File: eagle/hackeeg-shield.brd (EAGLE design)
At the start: 101.6 x 53.3 mm, 144 parts, among them IC1 ADS1299IPAG, IC10 TXB0108PWR, IC11 TXB0108PWR, IC2 TPS72325DBVT, IC3 TPS73225DBVT, IC5 24AA256UID, IC6 TPS60403DBVT, IC7 OPA376DBV, IC8 OPA376DBV, IC9 TXS0102DCUR

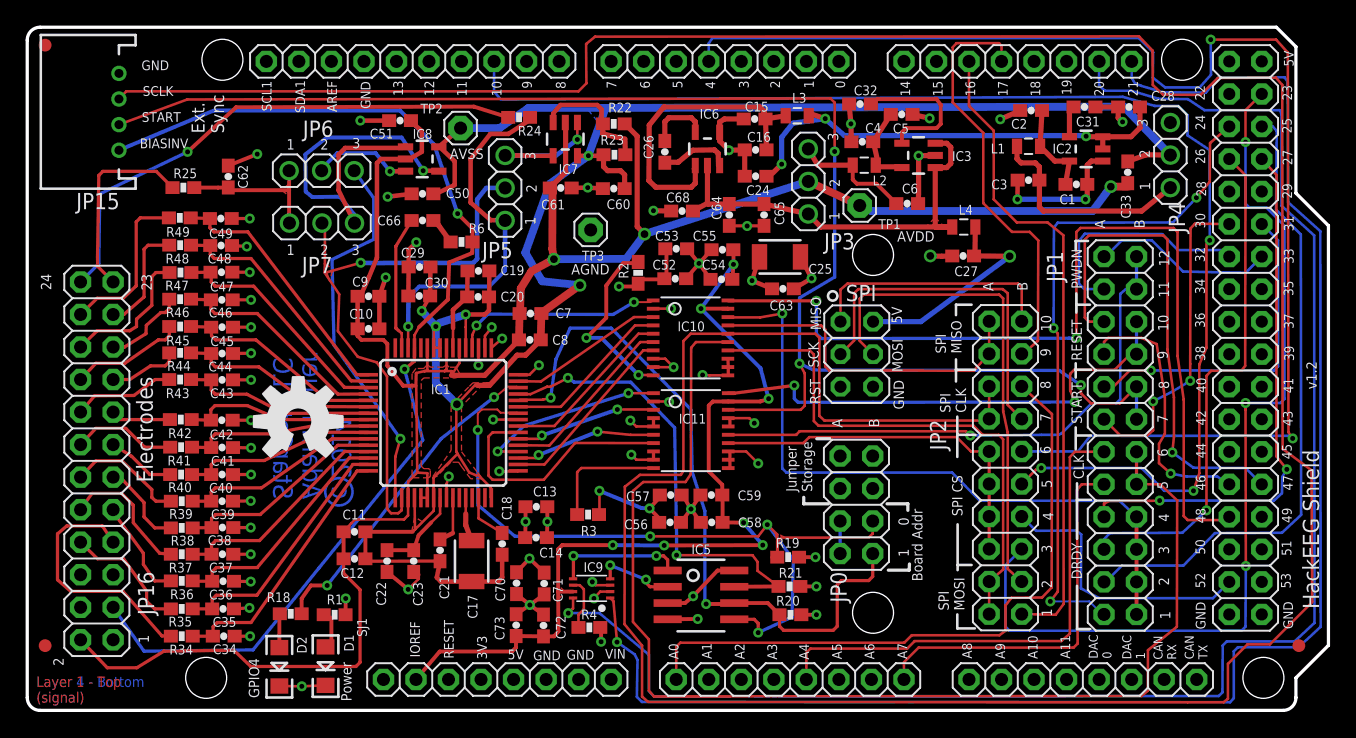
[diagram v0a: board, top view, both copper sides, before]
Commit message: changed inner layer (AGND and DVDD) polygon isolate clearance to 12 mils (from 0)
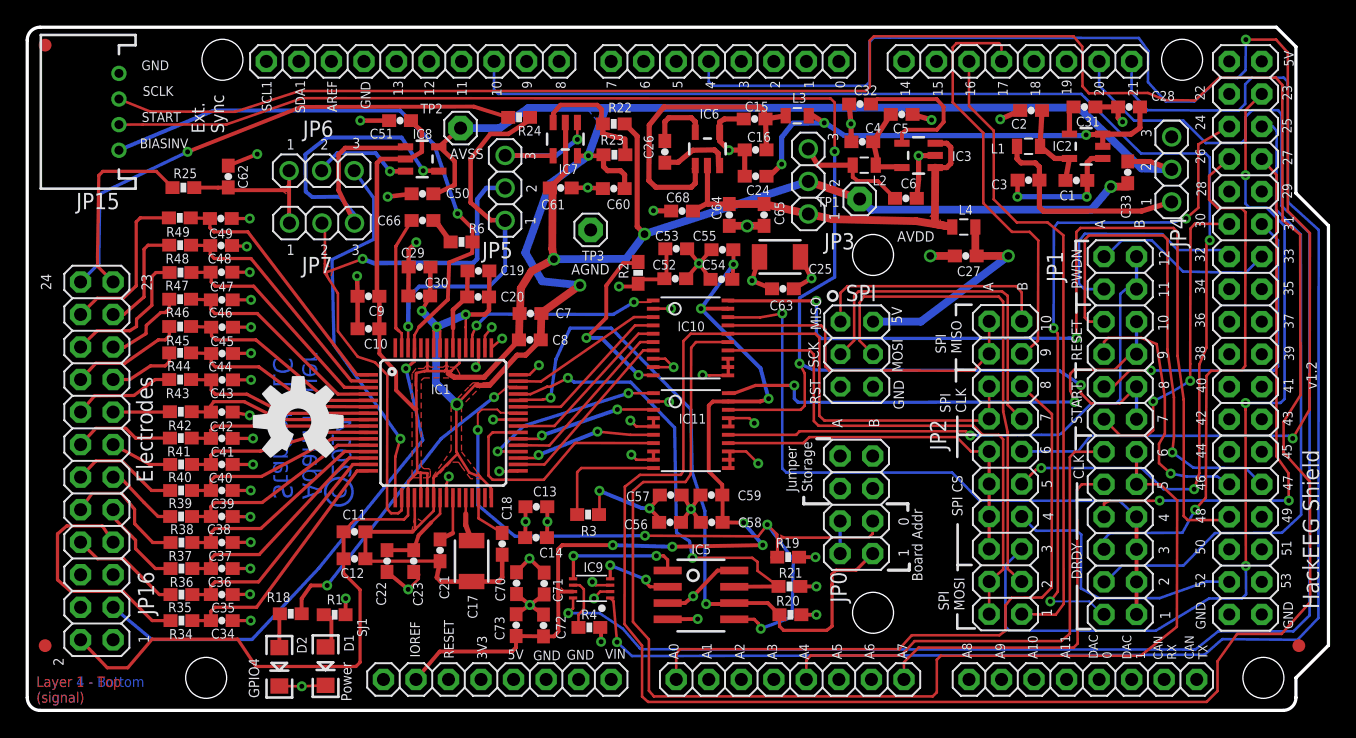
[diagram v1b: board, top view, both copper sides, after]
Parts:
- moved C34 1.23 mm to (15.3, 7.14)
- moved R34 1.22 mm to (12.2, 7.14)
- moved JP4 1.12 mm to (89.5, 42.4)
- moved C35 1.12 mm to (15.3, 9.17)
- moved R35 1.12 mm to (12.2, 9.17)
- moved C36 1.00 mm to (15.3, 11.2)
- moved R36 0.97 mm to (12.2, 11.2)
- moved C37 0.92 mm to (15.3, 13.2)
- moved R37 0.91 mm to (12.2, 13.2)
- moved R38 0.89 mm to (12.1, 15.3)
- moved C38 0.87 mm to (15.3, 15.3)
- moved R39 0.84 mm to (12.1, 17.3)
- moved C39 0.84 mm to (15.3, 17.3)
- moved C40 0.79 mm to (15.3, 19.3)
- moved R40 0.79 mm to (12.1, 19.3)
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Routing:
- net !ADC_CS_0: track 105.3 -> 110.8 mm
- net ARD_SCL: track 125.0 -> 120.3 mm
- net ARD_SDA: track 125.9 -> 121.6 mm
- net AVDD: track 177.8 -> 180.3 mm
- net ADC_DRDY_2: track 40.2 -> 42.5 mm
- net !ADC_CS_3: track 72.6 -> 70.8 mm
- net AVSS: track 172.5 -> 174.2 mm
- net ADS_SPI_CLK: track 262.8 -> 264.5 mm
- net BIASINV: track 86.8 -> 85.2 mm
- net !ADC_CS_1: track 102.4 -> 101.1 mm
- net IN1N: track 9.91 -> 8.71 mm
- net AGND: track 148.4 -> 149.5 mm
- net IN3P: track 6.79 -> 5.71 mm
- net AIN1N: track 19.8 -> 18.9 mm
- net ADC_DRDY_3: track 42.1 -> 42.9 mm
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- removed copper zone on layer 15, net N$43
- removed copper zone on layer 15, net N$44
- removed copper zone on layer 15, net N$47
- removed copper zone on layer 2, net N$56
- removed copper zone on layer 2, net N$57

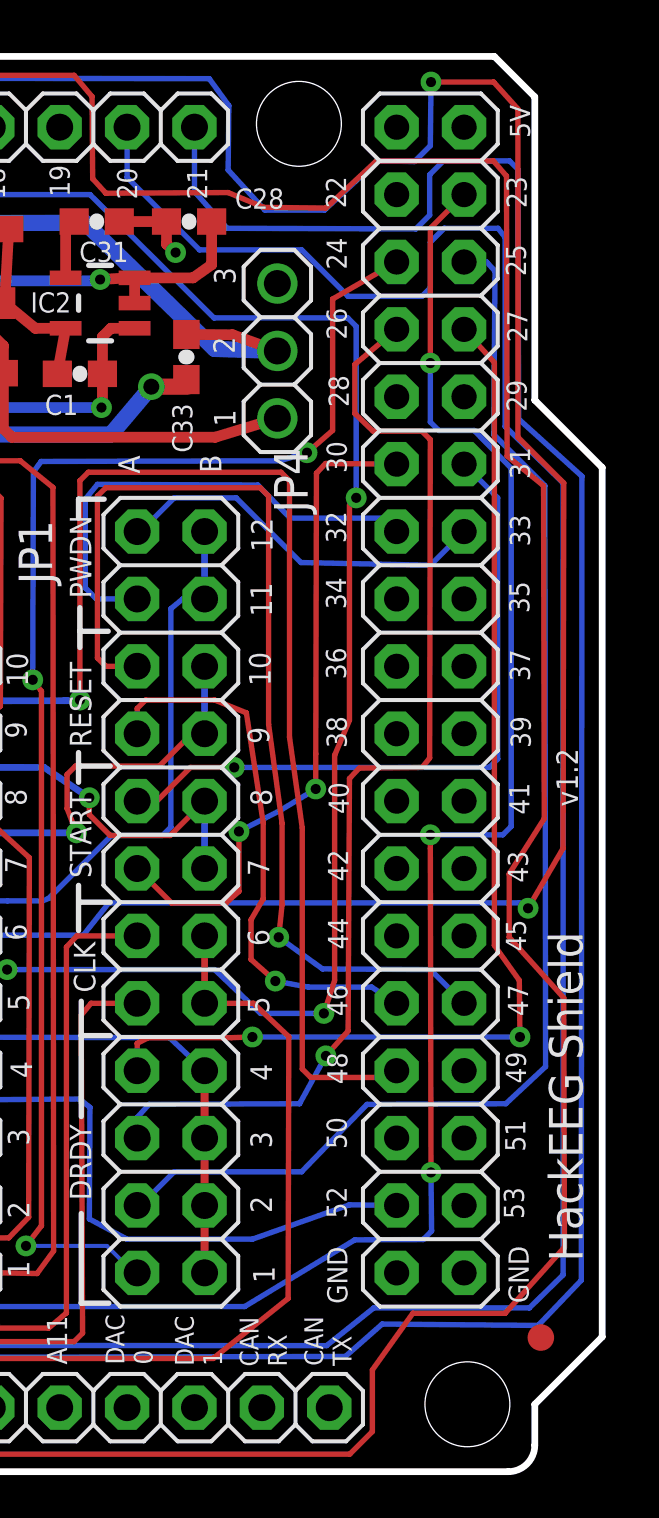
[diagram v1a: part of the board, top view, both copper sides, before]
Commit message: updated cam file to have better clearances; changed routing to avoid congestion and close traces on right edge of board toop and bottom
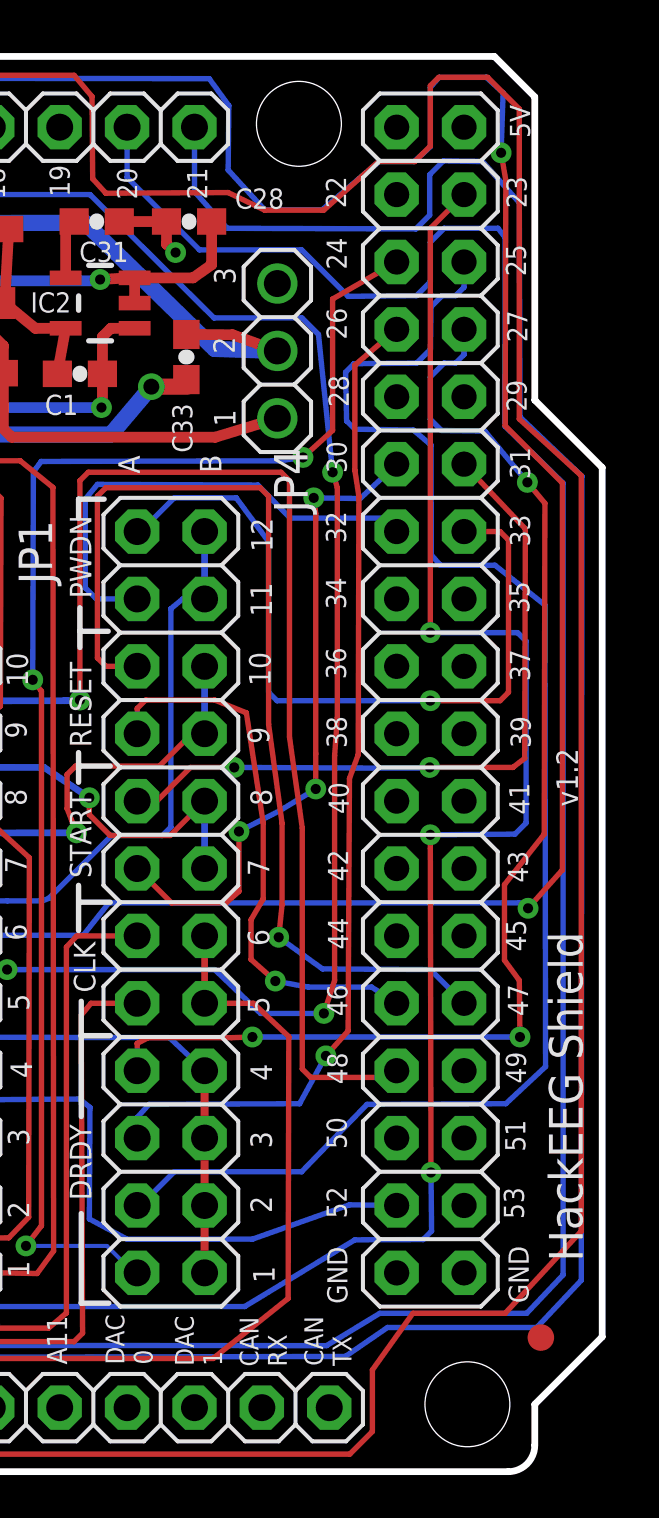
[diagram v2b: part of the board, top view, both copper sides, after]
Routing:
- net !ADC_PWDN_1: track 14.4 -> 28.8 mm, vias 0 -> 1
- net ADC_DRDY_1: track 49.6 -> 57.1 mm
- net ADS_SPI_CLK: track 264.5 -> 269.9 mm
- net ADC_DRDY_2: track 42.5 -> 37.7 mm
- net ADC_DRDY_3: track 42.9 -> 46.3 mm, vias 2 -> 3
- net !ADC_CS_3: track 70.8 -> 72.7 mm
- net !ADC_CS_1: track 101.1 -> 99.3 mm
- net ADC_START_1: track 25.9 -> 27.3 mm, vias 1 -> 2
- net ARD_SCL: track 120.3 -> 119.4 mm
- net ADC_START_0: track 25.2 -> 24.7 mm, vias 2 -> 3

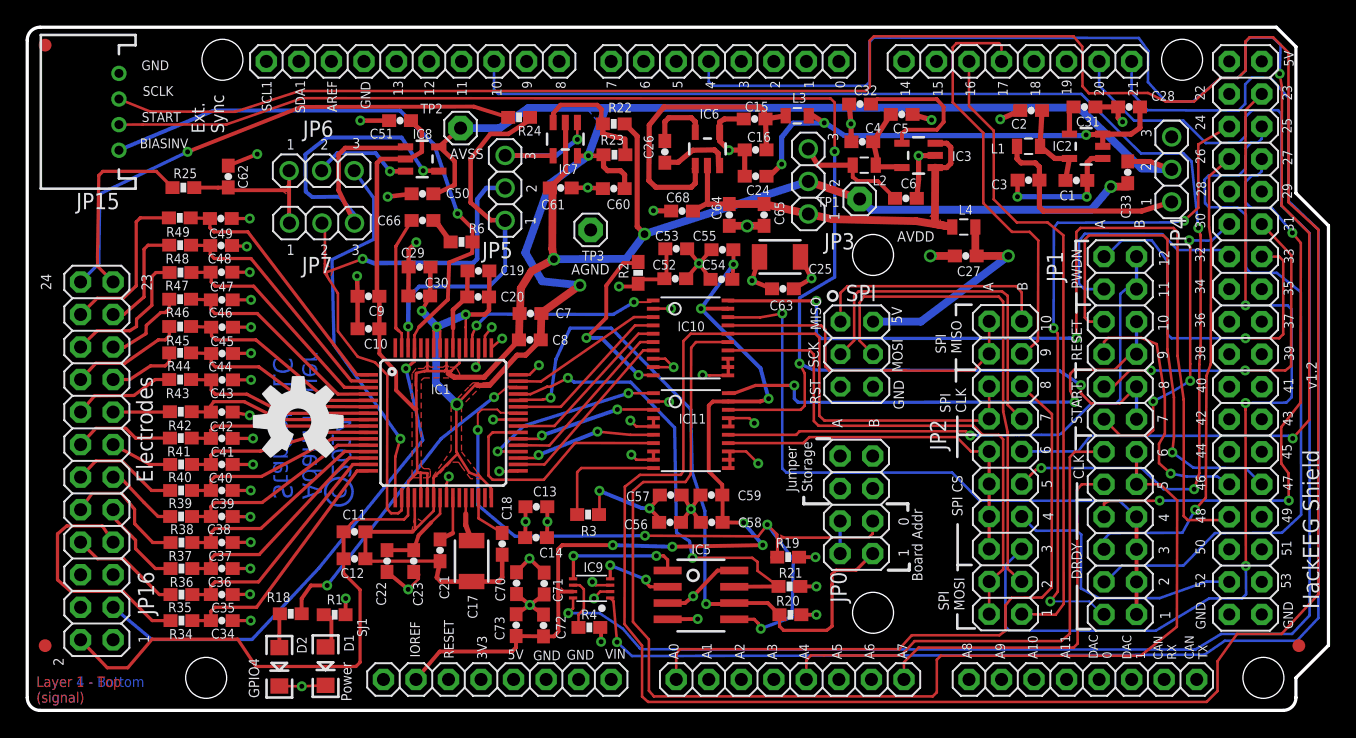
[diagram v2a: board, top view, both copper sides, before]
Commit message: changed rest-rings to min 12mil and fixed all DRC errors
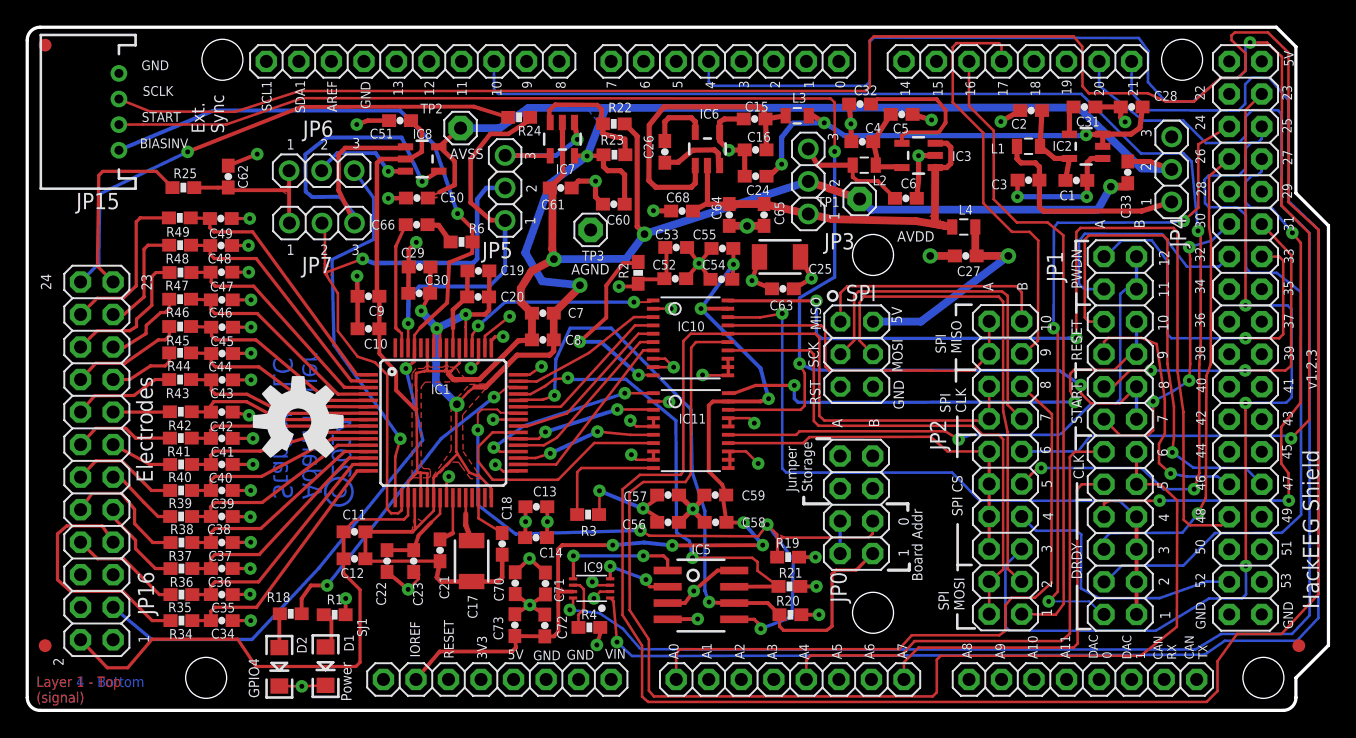
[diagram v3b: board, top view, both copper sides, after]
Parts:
- moved C60 1.22 mm to (45.9, 39.6)
- moved C8 1.02 mm to (40.4, 29.1)
- moved C7 0.97 mm to (40.4, 31.1)
- moved C66 0.56 mm to (30.5, 38.0)
- moved C50 0.54 mm to (30.6, 40.1)
- moved C59 0.30 mm to (53.8, 16.9)
- moved C58 0.30 mm to (53.9, 14.8)
- moved IC7 0.23 mm to (41.9, 44.7)
- moved C57 0.20 mm to (50.2, 16.9)
- moved C28 0.20 mm to (86.4, 47.2)
- moved C30 0.20 mm to (30.7, 32.7)
- moved C56 0.15 mm to (50.2, 14.8)
- moved C70 0.10 mm to (38.2, 10.1)
- moved C72 0.10 mm to (40.5, 6.76)
- moved C53 0.10 mm to (50.8, 36.3)
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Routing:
- net AGND: track 149.5 -> 153.5 mm
- net AVSS: track 174.2 -> 177.6 mm
- net DVDD: track 39.5 -> 42.1 mm
- net ADS_SPI_CLK: track 269.9 -> 272.0 mm
- net !ADC_CS_0: track 110.9 -> 109.8 mm
- net N$17: track 31.7 -> 32.7 mm
- net AVDD: track 180.3 -> 181.2 mm
- net N$561: track 14.5 -> 15.4 mm
- net !ADC_PWDN_0: track 18.2 -> 19.0 mm
- net ARD_SDA: track 121.4 -> 120.8 mm
- net ADC_START_0: track 24.7 -> 24.2 mm
- net ADS_CLKSEL: track 72.4 -> 72.9 mm
- net N$25: track 10.5 -> 9.99 mm
- removed copper zone on layer 15, net N$32
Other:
- board text added: "Layer 3 DVDD (+)"
- board text added: "v1.2.3"
- board text removed: "Layer 3 - DVDD (+)"
- board text removed: "v1.2"

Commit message: updated layer AGND and DVDD text to have larger widths and enclosing cutout box to prevent clearance errors
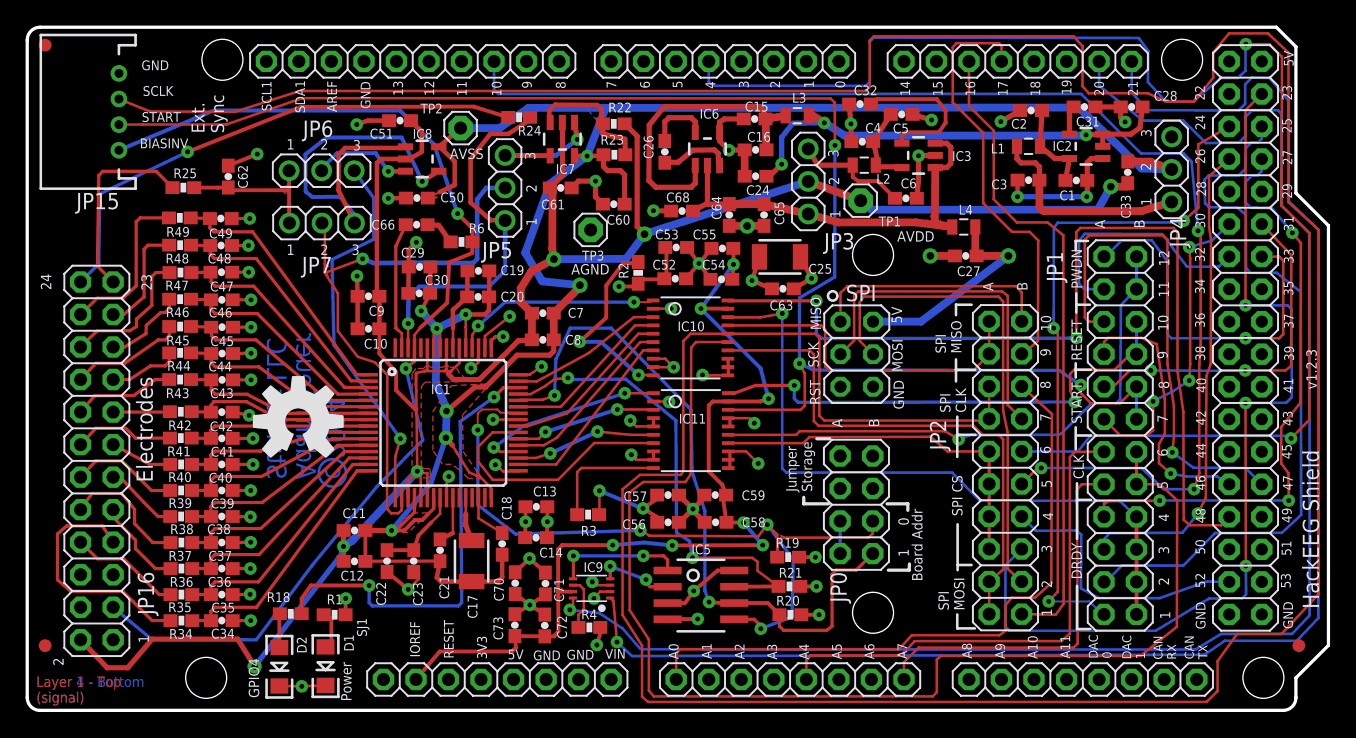
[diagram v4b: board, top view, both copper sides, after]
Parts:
- moved C12 0.20 mm to (25.7, 11.8)
- moved TP1 0.15 mm to (65.2, 39.9)
- moved C11 0.10 mm to (25.7, 14.2)
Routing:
- net GPIO4: track 25.9 -> 35.7 mm
- net AVSS: track 177.6 -> 183.1 mm, vias 6 -> 8
- net AVDD: track 181.2 -> 176.9 mm, vias 3 -> 6
- net ADS_SPI_CLK: track 272.0 -> 270.2 mm
- net !ADS_PWDN: track 44.3 -> 43.7 mm
- added copper zone on layer 15, net N$43
- added copper zone on layer 2, net N$43
- removed copper zone on layer 2, net N$58

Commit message: widened AVDD and AVSS trace widths and improved routing
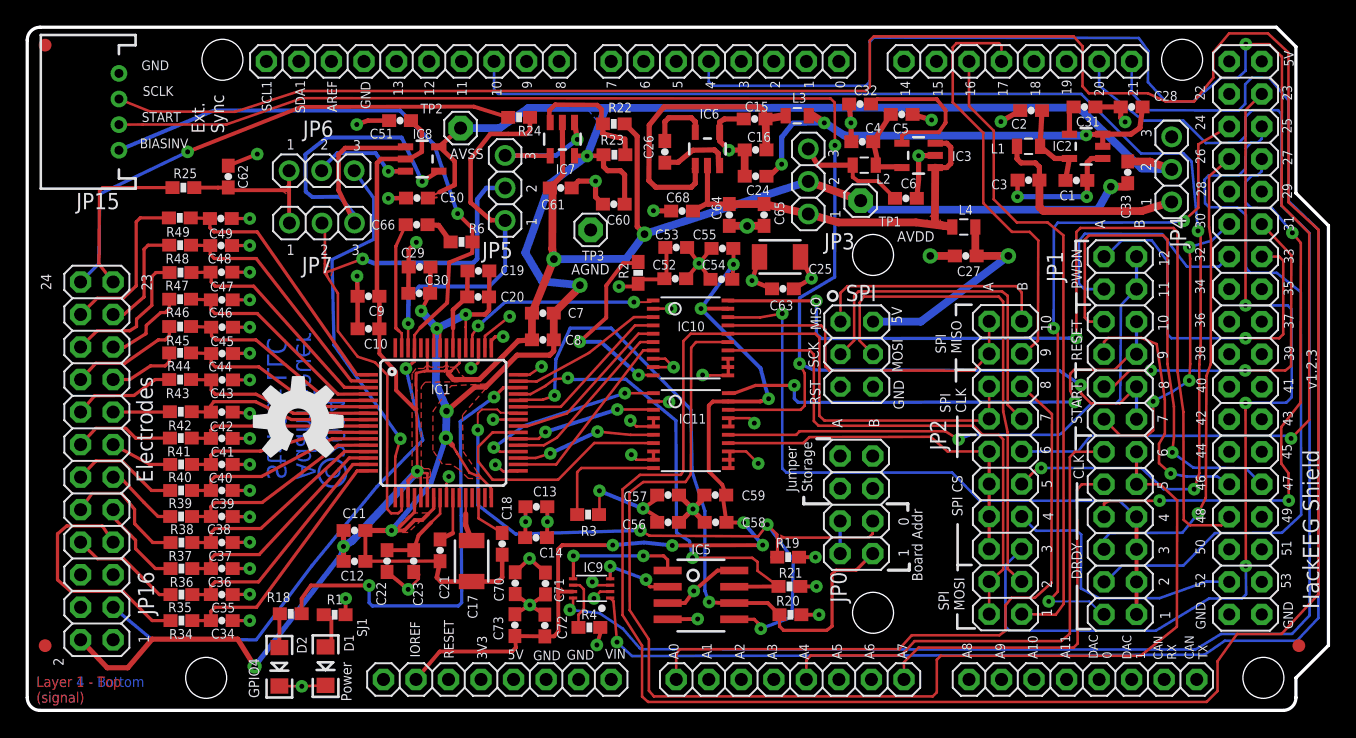
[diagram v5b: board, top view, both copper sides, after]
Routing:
- net REF_ELEC_CON: track 15.2 -> 13.3 mm
- net AVDD: track 176.9 -> 175.6 mm
- net AGND: track 153.5 -> 152.4 mm
- net BIAS_ELEC: track 29.6 -> 30.3 mm

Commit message: updated board version number to 1.2.4
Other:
- board text added: "v1.2.4"
- board text removed: "v1.2.3"
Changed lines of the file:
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@@
 StarCat LLC</text>
 <circle x="23.9522" y="18.669" radius="1.0668" width="0.2032" layer="16"/>
-<text x="100.8126" y="25.1968" size="0.8128" layer="21" font="vector" ratio="12" rot="R90">v1.2.3</text>
+<text x="100.8126" y="25.1968" size="0.8128" layer="21" font="vector" ratio="12" rot="R90">v1.2.4</text>
 <wire x1="97.663" y1="53.467" x2="99.187" y2="51.943" width="0.254" layer="20"/>
 <wire x1="99.187" y1="40.513" x2="101.727" y2="37.973" width="0.254" layer="20"/>
